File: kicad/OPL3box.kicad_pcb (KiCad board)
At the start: 2 copper layers, 81.9 x 44.5 mm, 45 parts, among them J1 MIDI-IN, J2 6-12V DC, J3 Line Out, Q1 2N3904, SW1 Encoder, U1 Arduino_Pro_Micro, U2 6N138, U3 128x32_OLED, U4 OPL3_YMF262_M, U5 YAC512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

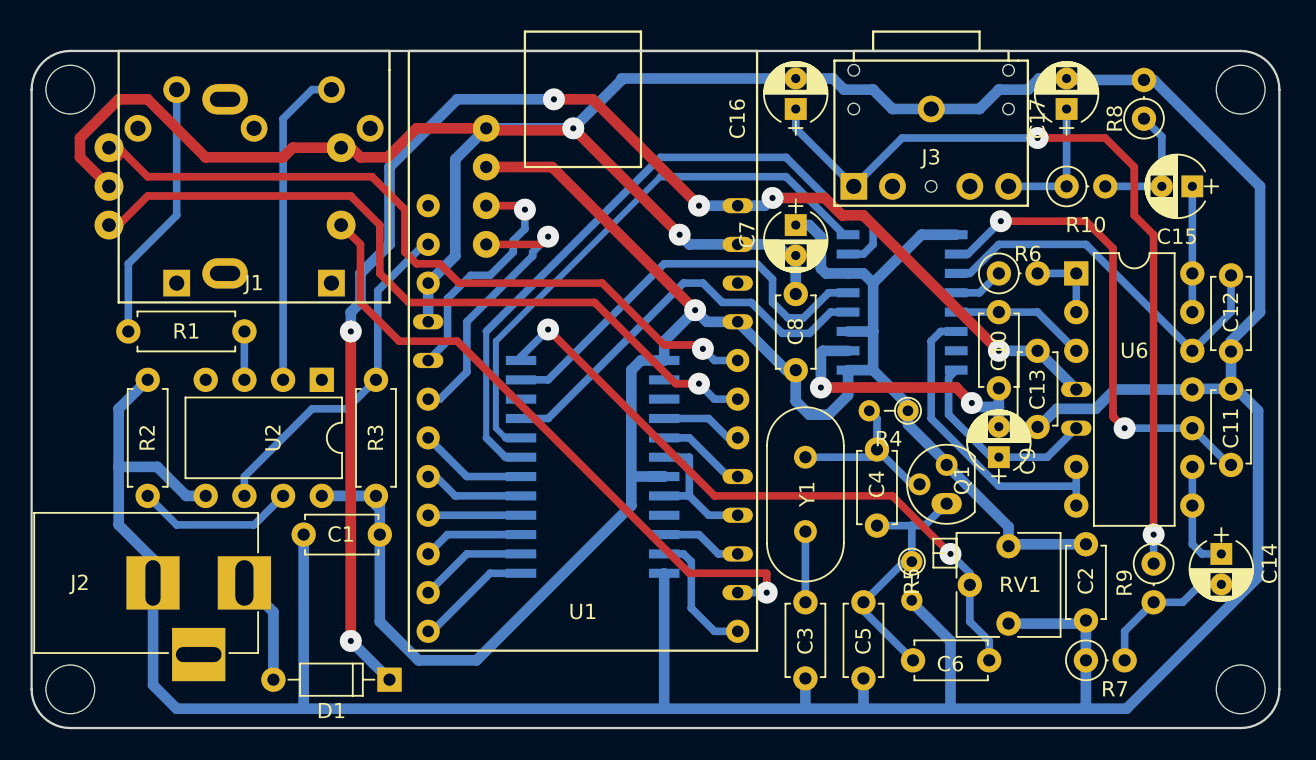
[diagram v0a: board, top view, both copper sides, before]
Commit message: PCB: fix the flipped the MIDI connector issue
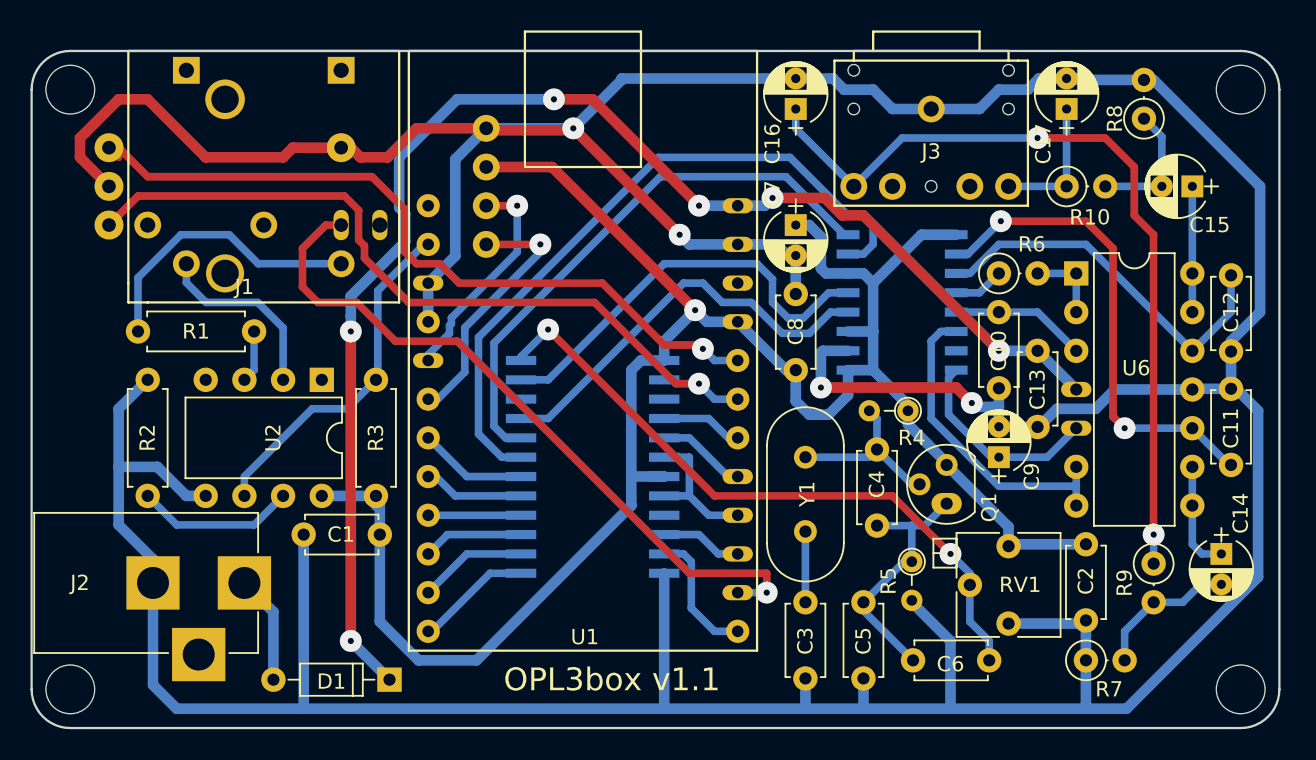
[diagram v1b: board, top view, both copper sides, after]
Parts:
- moved J1 14.0 mm to (31.1, 17.8), turned to 180 degrees
- moved R1 0.64 mm to (30.5, 34.9)
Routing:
- net Net-(J1-Pad4): track 21.1 -> 12.2 mm
- net ENCSW: track 43.6 -> 47.9 mm
- net Net-(J1-Pad5): track 17.2 -> 18.8 mm
- net SDA: track 18.7 -> 17.1 mm
- net SCK: track 15.9 -> 14.6 mm
- net Net-(U4-Pad19): track 44.9 -> 45.6 mm
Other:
- rule pad_to_mask_clearance: 0.2 -> 0.1
- board text added: "OPL3box v1.1"
